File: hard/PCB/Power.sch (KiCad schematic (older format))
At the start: 65 parts, among them P3 CONN_02X02, P4 CONN_02X02, P6 CONN_01X03, P7 B6B-PH-K-S(LF)(SN), U2 TPS63070

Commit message: Update supply power
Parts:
- removed C10, C8: 10u, Capacitors_SMD:C_0603, symbol C
- removed C11, C12, C13: 22u, Capacitors_SMD:C_0805, symbol C
- removed C6, C7: 10u, Capacitors_SMD:C_0805, symbol C
- removed C9: 100n, Capacitors_SMD:C_0402, symbol C
- removed C? (x3): C, symbol C
- removed CF10, CF12, CF14, CF15, CF16, CF17, CF18, CF19, CF2, CF20, CF21, CF22, CF23, CF24, CF25, CF3, CF4, CF5, CF6, CF7, CF8, CF9: 0.1uF, opendous:SM0603, symbol C
- removed CF11, CF26, CF27: 1uF, opendous:SM0603, symbol C
- removed CF28, CF29: 4.7uF, opendous:SM1206_Opendous, symbol C
- removed CF32, CF33, CF35: 33uF, opendous:SM1206_Opendous, symbol C
- removed CF34: 100n, opendous:SM0603, symbol C
- removed L3: XFL4020-152ME, resonator:XFL4020, symbol INDUCTOR
- removed L?: L, symbol L
- removed R12: 10k, Resistors_SMD:R_0603, symbol R
- removed R13: 680k, Resistors_SMD:R_0603, symbol R
- removed R14: 130k, Resistors_SMD:R_0603, symbol R
- removed R15: 100k, Resistors_SMD:R_0603, symbol R
- removed R? (x3): R, symbol R
- removed U2: TPS63070, resonator:TPS63071, symbol TPS63071
- removed U?: TPS563208, TO_SOT_Packages_SMD:SOT-23-6, symbol TPS563208
- added C1: 10uF, Capacitors_SMD:C_1210, symbol C
- added C2: 100nF, Capacitors_SMD:C_0603, symbol C
- added C3: 22uF, Capacitors_SMD:C_0805, symbol C
- added C4: 3.3nF, Capacitors_SMD:C_0603, symbol C
- added CS10, CS11, CS21, CS22, CS23, CS24, CS25, CS26, CS27, CS28, CS29, CS30, CS31, CS32, CS33, CS8, CS9: 0.1uF, Resistors_SMD:R_0603, symbol C
- added CS12, CS14, CS15, CS16, CS17, CS18, CS19, CS34: 1uF, Resistors_SMD:R_0603, symbol C
- added CS20, CS35: 4.7uF, Resistors_SMD:R_1206, symbol C
- added CS3, CS4, CS6: 33uF, Resistors_SMD:R_1206, symbol C
- added CS5: 100n, Resistors_SMD:R_0603, symbol C
- added L1: VLS5045EX-2R2N, Inductors:Inductor_Taiyo-Yuden_NR-50xx, symbol L
- added R1: 0R, Resistors_SMD:R_0402, symbol R
- added U2: TPS62133RGTR, Project:QFN16, symbol TPS6213x
- CS1: renamed from CF30; footprint opendous:SM1206_Opendous -> Resistors_SMD:R_1206
- CS13: renamed from CF13; footprint opendous:SM1206_Opendous -> Resistors_SMD:R_1206
- CS2: renamed from CF31; footprint opendous:SM0603 -> Resistors_SMD:R_0603
- CS7: renamed from CF1; footprint opendous:SM0603 -> Resistors_SMD:R_0603
- PS1: footprint Connect:JACK_ALIM -> Project:JACK_ALIM
- S1: value 9077-1 -> POWER; footprint resonator:CKCOMP-OS102011MA1QN1 -> Project:CKCOMP-OS102011MA1QN1
- U3: renamed from UF2; footprint SMD_Packages:SOT-223 -> Project:SOT-223
- U4: renamed from UF3; footprint SMD_Packages:SOT-223 -> Project:SOT-223
- renumbered P3 to PW1, P4 to PW2, P7 to PW_LCD1
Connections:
- net labels added: PG, VCC
- net labels removed: +9V0
- wire segments 194 -> 171
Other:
- note added: "9077-1\n"
- note added: "Conector para seleccionar fuente \npor medio de un jumper.\n\n> VDD5V: 5VDC del TPS62133\n> +5V: Referencia de 5VDC de \n toda la tarjeta.\n> USBVCC: 5VDC del conector \n USB"
- note added: "Jumper to select \noperating frequency,\nsee datasheet."
- note added: "Power LCD\n"
- note removed: "Conector para seleccionar fuente \npor medio de un jumper.\n\n> VDD5V: Fuente jack DC de 9VDC \n a 5VDC.\n> +5V: Referencia de 5VDC de toda \n la tarjeta.\n> USBVCC: 5VDC obtenido por \n conector USB"
- moved on the sheet: CS1, CS13, CS2, CS7, P6, PS1, PW_LCD1, S1, U3, U4

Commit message: Corrección esquematico
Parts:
- removed CS11, CS26, CS28, CS30, CS31, CS32, CS33: 0.1uF, Resistors_SMD:R_0603, symbol C
- added C10, C7, C8: 33uF, Capacitors_SMD:C_1206, symbol C
- added C9: 100n, Capacitors_SMD:C_0603, symbol C
- added CS12, CS2, CS7: 0.1uF, Capacitors_SMD:C_0603, symbol C
- C5: renamed from CS1; footprint Resistors_SMD:R_1206 -> Capacitors_SMD:C_1206
- C6: renamed from CS2; footprint Resistors_SMD:R_0603 -> Capacitors_SMD:C_0603
- CS1: renamed from CS7; footprint Resistors_SMD:R_0603 -> Capacitors_SMD:C_0603
- CS10, CS21, CS22, CS23, CS24, CS25, CS8, CS9: footprint Resistors_SMD:R_0603 -> Capacitors_SMD:C_0603
- CS11: renamed from CS12; footprint Resistors_SMD:R_0603 -> Capacitors_SMD:C_0603
- CS13: footprint Resistors_SMD:R_1206 -> Capacitors_SMD:C_1206
- CS14, CS15, CS16, CS17, CS18, CS19: value 1uF -> 0.1uF; footprint Resistors_SMD:R_0603 -> Capacitors_SMD:C_0603
- CS20: value 4.7uF -> 0.1uF; footprint Resistors_SMD:R_1206 -> Capacitors_SMD:C_0603
- CS26: renamed from CS34; footprint Resistors_SMD:R_0603 -> Capacitors_SMD:C_0603
- CS27: value 0.1uF -> 1uF; footprint Resistors_SMD:R_0603 -> Capacitors_SMD:C_0603
- CS28: renamed from CS35; footprint Resistors_SMD:R_1206 -> Capacitors_SMD:C_1206
- CS29: value 0.1uF -> 4.7uF; footprint Resistors_SMD:R_0603 -> Capacitors_SMD:C_1206
- CS3, CS4, CS6: value 33uF -> 0.1uF; footprint Resistors_SMD:R_1206 -> Capacitors_SMD:C_0603
- CS5: value 100n -> 0.1uF; footprint Resistors_SMD:R_0603 -> Capacitors_SMD:C_0603
- renumbered C4 to C3, C3 to C4, P6 to P1

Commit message: update 3d models
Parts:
- renumbered C3 to C10, C4 to C3, C5 to C4, C6 to C5, C7 to C6, C8 to C7, C9 to C8, C10 to C9, CS21 to CS10, CS23 to CS11, CS25 to CS12, CS27 to CS13, CS29 to CS14, CS2 to CS15, CS4 to CS16, CS6 to CS17, CS8 to CS18, CS10 to CS19, CS3 to CS2, CS12 to CS20, CS14 to CS21, CS15 to CS22, CS16 to CS23, CS18 to CS24, CS20 to CS25, CS22 to CS26, CS24 to CS27, CS26 to CS28, CS28 to CS29, CS5 to CS3, CS7 to CS4, CS9 to CS5, CS11 to CS6, CS13 to CS7, CS17 to CS8, CS19 to CS9, P1 to P2

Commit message: update layout
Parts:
- removed PW1, PW2: CONN_02X02, Socket_Strips:Socket_Strip_Straight_2x02_Pitch2.54mm, symbol CONN_02X02
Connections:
- wire segments 171 -> 155

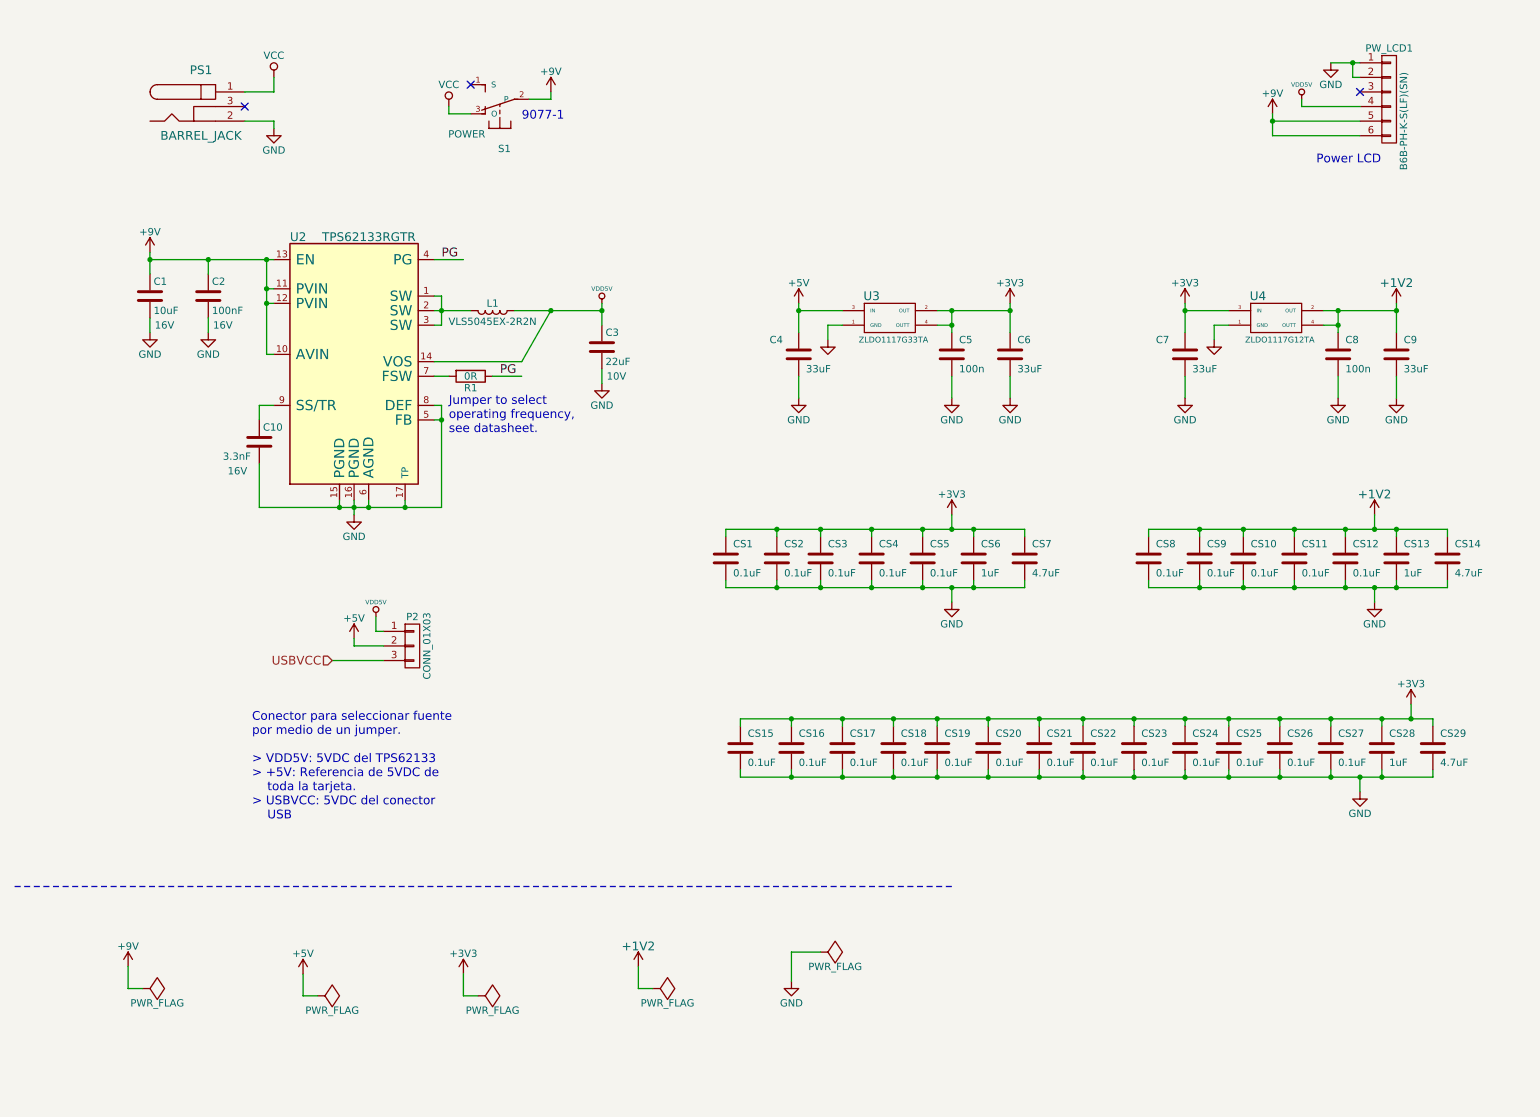
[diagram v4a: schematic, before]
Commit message: Add jmp Rpi Power
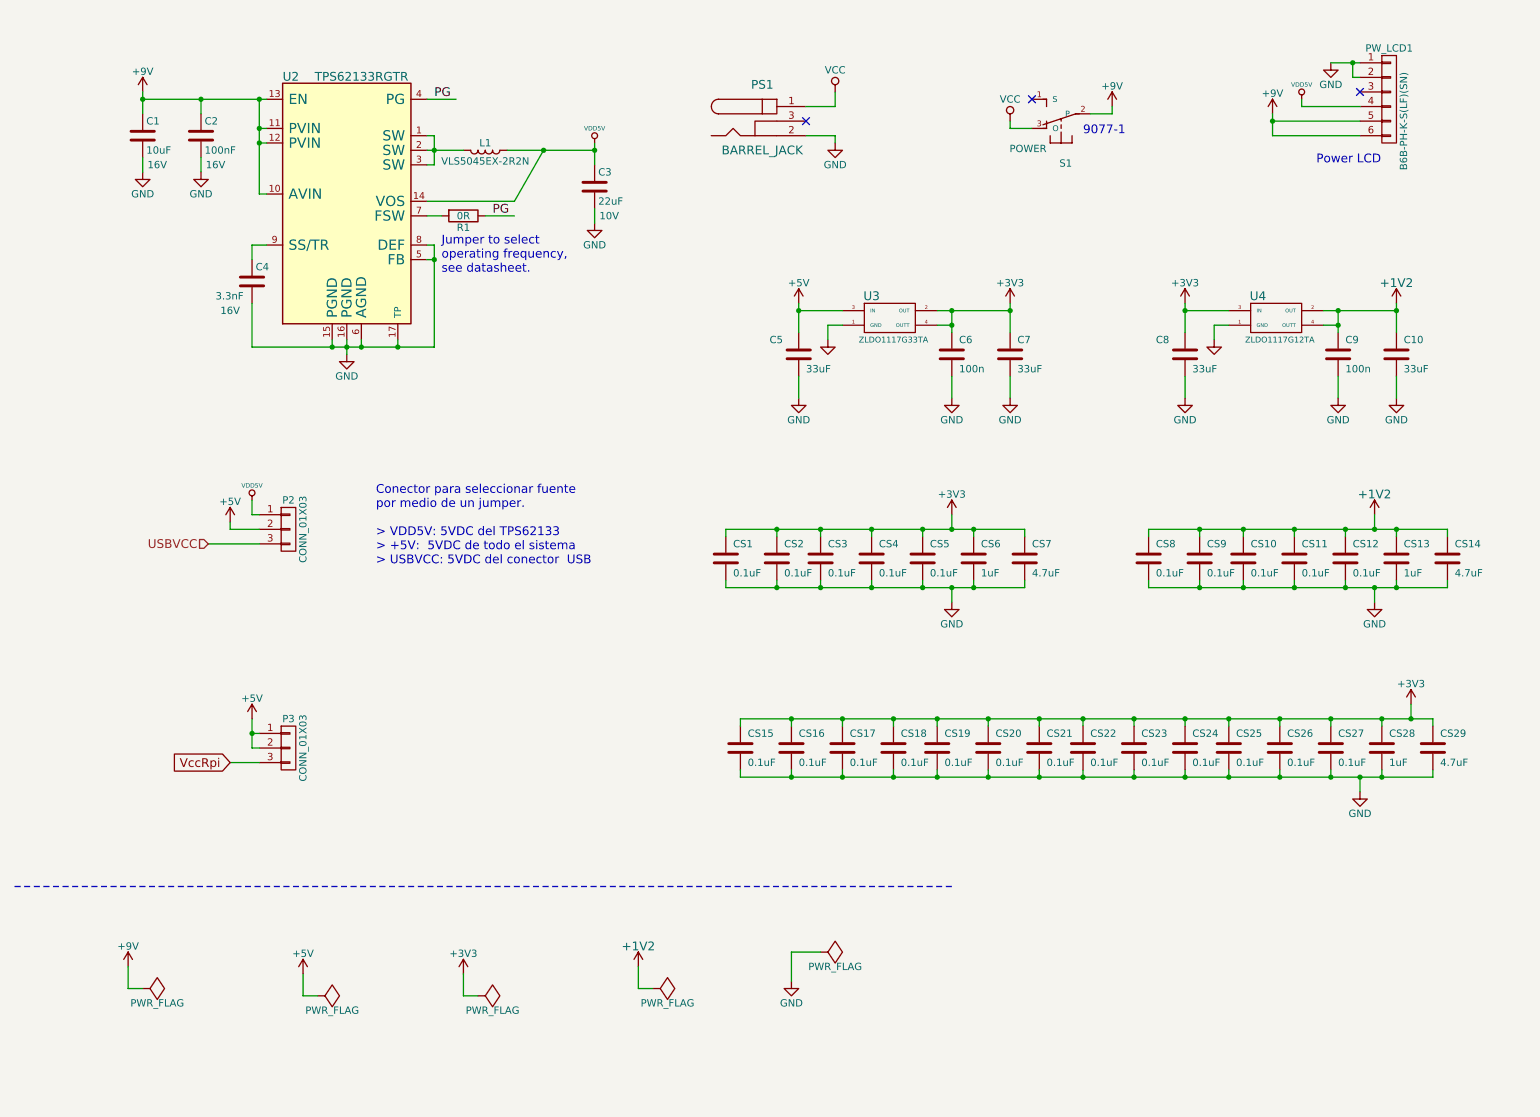
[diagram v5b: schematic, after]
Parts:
- added P3: CONN_01X03, Socket_Strips:Socket_Strip_Straight_1x03_Pitch2.54mm, symbol CONN_01X03
- renumbered C9 to C10, C10 to C4, C4 to C5, C5 to C6, C6 to C7, C7 to C8, C8 to C9
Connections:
- net +5V: now also P3.1 (P1), P3.2 (P2)
- new net VccRpi: P3.3 (P3)
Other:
- note added: "Conector para seleccionar fuente \npor medio de un jumper.\n\n> VDD5V: 5VDC del TPS62133\n> +5V: 5VDC de todo el sistema\n> USBVCC: 5VDC del conector USB"
- note removed: "Conector para seleccionar fuente \npor medio de un jumper.\n\n> VDD5V: 5VDC del TPS62133\n> +5V: Referencia de 5VDC de \n toda la tarjeta.\n> USBVCC: 5VDC del conector \n USB"
- moved on the sheet: C1, C2, C3, C4, L1, P2, PS1, R1, S1, U2

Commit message: config power
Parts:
- removed P2: CONN_01X03, Socket_Strips:Socket_Strip_Straight_1x03_Pitch2.54mm, symbol CONN_01X03
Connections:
- net +5V: now also S1.2 (P)
- net +9V: now also PS1.1; no longer S1.2 (P)
- net GND: now also PS1.3
- net USBVCC: now also S1.3 (O)
- net VDD5V: now also S1.1 (S)
- removed net VCC: PS1.1, S1.3 (O)
- no-connect marks 3 -> 1
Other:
- moved on the sheet: S1

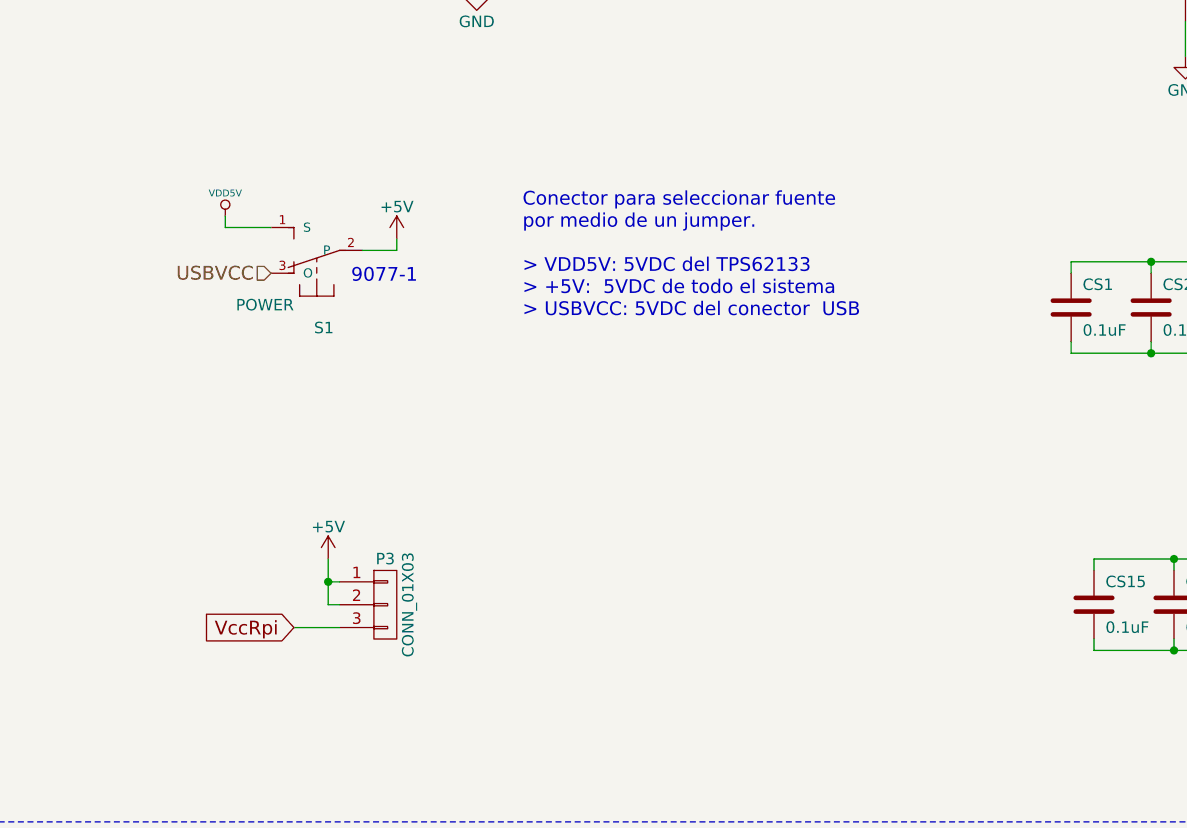
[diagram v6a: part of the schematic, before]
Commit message: se modifican el pin hdmi- las resitencias RN1 - eñ conector de  voltaje
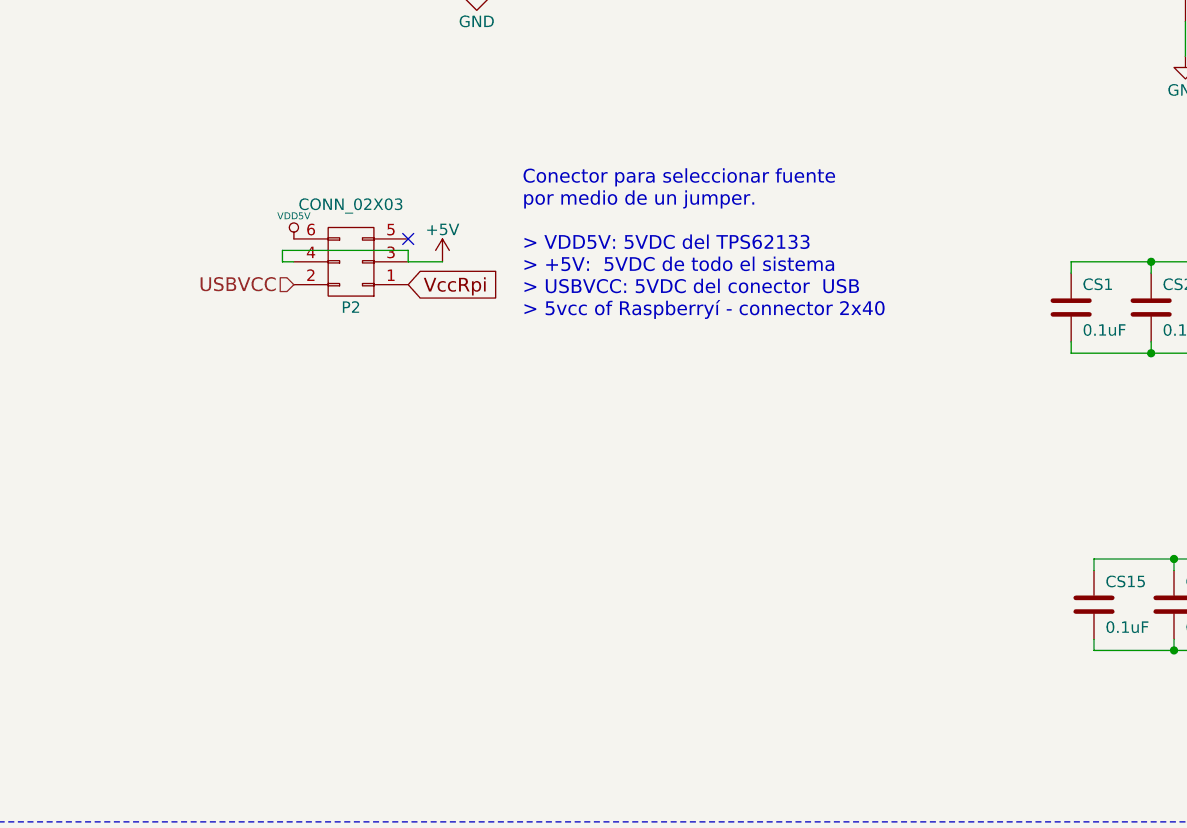
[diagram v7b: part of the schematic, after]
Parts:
- removed P3: CONN_01X03, Socket_Strips:Socket_Strip_Straight_1x03_Pitch2.54mm, symbol CONN_01X03
- removed S1: POWER, Project:CKCOMP-OS102011MA1QN1, symbol 9077-1
- added P2: CONN_02X03, Pin_Headers:Pin_Header_Straight_2x03_Pitch2.54mm, symbol CONN_02X03
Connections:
- net +5V: now also P2.3 (P3), P2.4 (P4)
- net USBVCC: now also P2.2 (P2)
- net VDD5V: now also P2.6 (P6)
- net VccRpi: now also P2.1 (P1)
- no-connect marks 1 -> 2
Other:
- note added: "Conector para seleccionar fuente \npor medio de un jumper.\n\n> VDD5V: 5VDC del TPS62133\n> +5V: 5VDC de todo el sistema\n> USBVCC: 5VDC del conector USB\n> 5vcc of Raspberryí - connector 2x40"
- note removed: "9077-1\n"
- note removed: "Conector para seleccionar fuente \npor medio de un jumper.\n\n> VDD5V: 5VDC del TPS62133\n> +5V: 5VDC de todo el sistema\n> USBVCC: 5VDC del conector USB"
